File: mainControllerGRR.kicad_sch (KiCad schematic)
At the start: 36 parts, among them IC1 L7805CD2T-TR, IC2 L7805CD2T-TR, IC3 LD1086D2T33TR, J1 Raspberry_Pi_2_3, J2 XT60PW-M, J3 XT60PW-M, J4 XT30PW-M, J42 Conn_01x02, J5 XT30PW-M, J6 Conn_01x02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

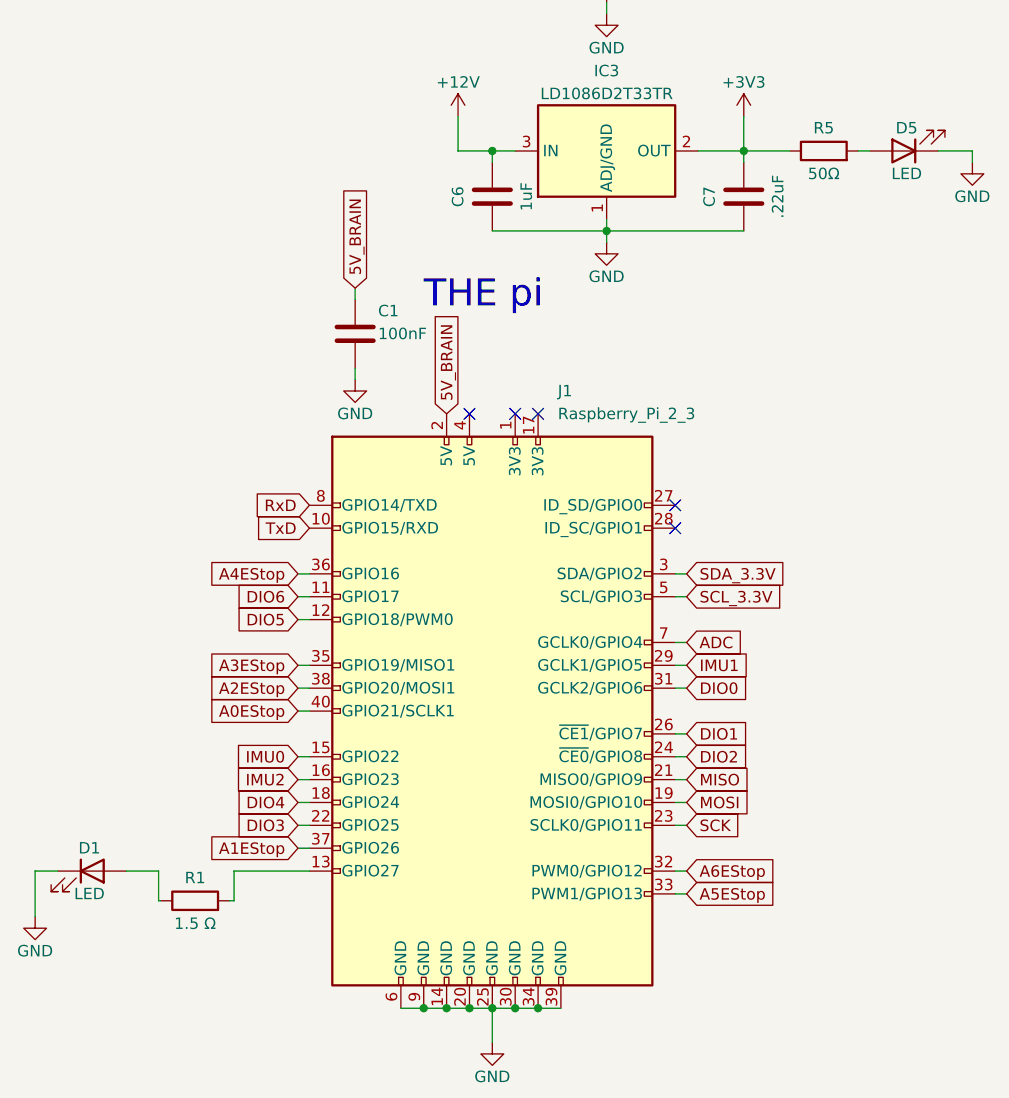
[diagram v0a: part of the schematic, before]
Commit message: working on adding JLC part numbers
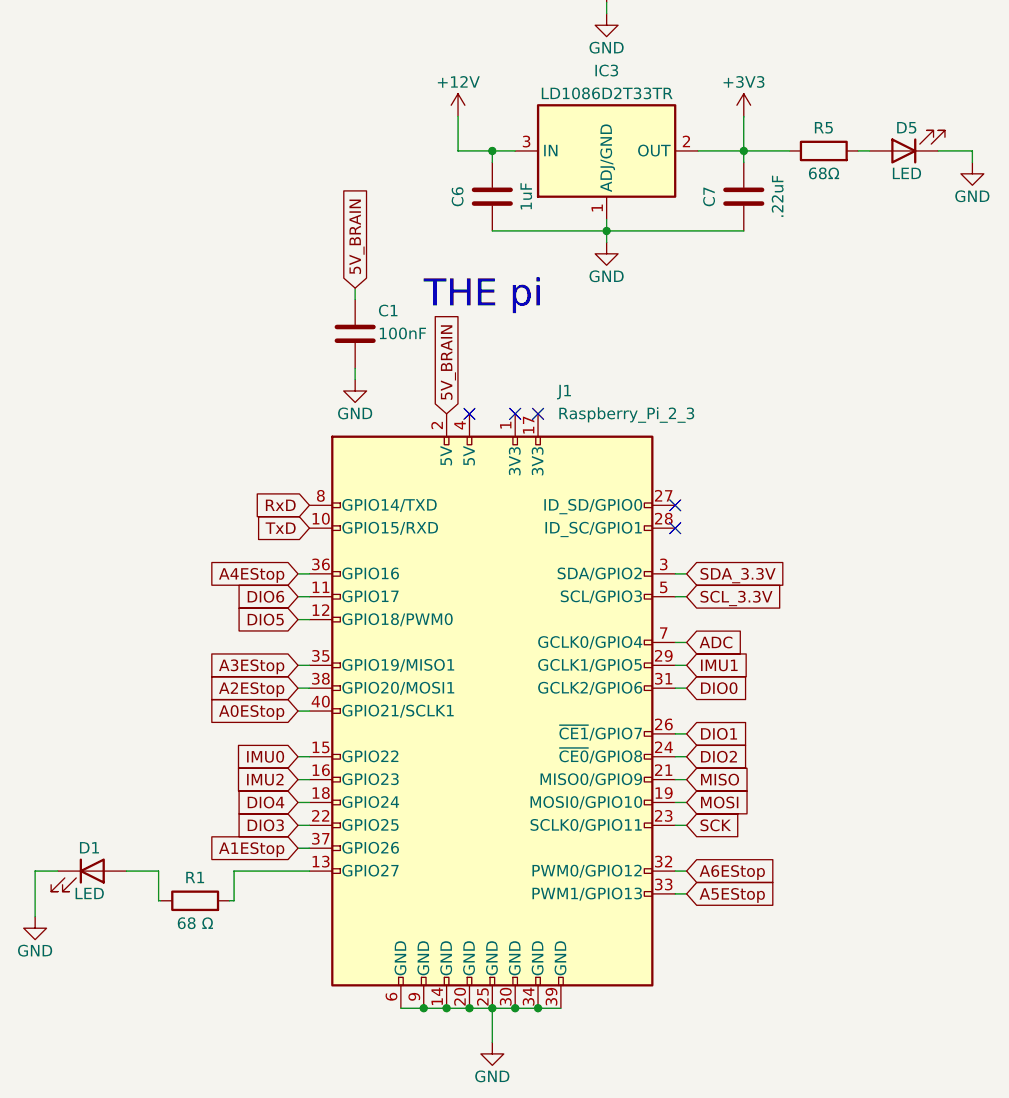
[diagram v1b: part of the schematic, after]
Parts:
- D1, D2, D3, D4, D5: LCSC (none) -> C125098
- R1: value 1.5 Ω -> 68 Ω; LCSC (none) -> C267560
- R2, R6: LCSC (none) -> C491139
- R3, R4: LCSC (none) -> C705726
- R5: value 50Ω -> 68Ω; LCSC (none) -> C267560
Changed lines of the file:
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@@
+      (effects (font (size 1.27 1.27)) hide)
+    )
+    (property "LCSC" "C125098" (at 78.74 22.86 0)
       (effects (font (size 1.27 1.27)) hide)
     )
@@
       (effects (font (size 1.27 1.27)) hide)
     )
+    (property "LCSC" "C125098" (at 25.4 171.45 0)
+      (effects (font (size 1.27 1.27)) hide)
+    )
     (pin "1")
     (pin "2")
@@
       (effects (font (size 1.27 1.27)))
     )
-    (property "Value" "1.5 Ω" (at 36.83 177.292 90)
+    (property "Value" "68 Ω" (at 36.83 177.292 90)
       (effects (font (size 1.27 1.27)))
     )
@@
       (effects (font (size 1.27 1.27)) hide)
     )
+    (property "LCSC" "C267560" (at 36.83 174.752 90)
+      (effects (font (size 1.27 1.27)) hide)
+    )
     (pin "1")
     (pin "2")
@@
     )
     (property "Datasheet" "~" (at 127 29.21 0)
+      (effects (font (size 1.27 1.27)) hide)
+    )
+    (property "LCSC" "C125098" (at 127 29.21 0)
       (effects (font (size 1.27 1.27)) hide)
     )
@@
       (effects (font (size 1.27 1.27)) hide)
     )
+    (property "LCSC" "C491139" (at 55.88 53.34 90)
+      (effects (font (size 1.27 1.27)) hide)
+    )
     (pin "1")
     (pin "2")
@@
       (effects (font (size 1.27 1.27)) hide)
     )
+    (property "LCSC" "C125098" (at 115.57 91.44 0)
+      (effects (font (size 1.27 1.27)) hide)
+    )
     (pin "1")
     (pin "2")
@@
       (effects (font (size 1.27 1.27)) hide)
     )
+    (property "LCSC" "C705726" (at 115.57 58.42 90)
+      (effects (font (size 1.27 1.27)) hide)
+    )
     (pin "1")
     (pin "2")
@@
       (effects (font (size 1.27 1.27)) hide)
     )
+    (property "LCSC" "C705726" (at 118.11 29.21 90)
+      (effects (font (size 1.27 1.27)) hide)
+    )
     (pin "1")
     (pin "2")
@@
     )
     (property "Datasheet" "~" (at 69.85 22.86 0)
+      (effects (font (size 1.27 1.27)) hide)
+    )
+    (property "LCSC" "C491139" (at 69.85 22.86 90)
       (effects (font (size 1.27 1.27)) hide)
     )
@@
       (effects (font (size 1.27 1.27)))
     )
-    (property "Value" "50Ω" (at 106.68 93.98 90)
+    (property "Value" "68Ω" (at 106.68 93.98 90)
       (effects (font (size 1.27 1.27)))
     )
@@
       (effects (font (size 1.27 1.27)) hide)
     )
+    (property "LCSC" "C267560" (at 106.68 91.44 90)
+      (effects (font (size 1.27 1.27)) hide)
+    )
     (pin "1")
     (pin "2")
@@
       (effects (font (size 1.27 1.27)) hide)
     )
+    (property "LCSC" "C125098" (at 124.46 58.42 0)
+      (effects (font (size 1.27 1.27)) hide)
+    )
